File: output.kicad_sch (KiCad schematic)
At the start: 76 parts, among them Q10 AO4407A, Q11 2N7002, Q12 MMBT3904, Q13 2N7002, Q14 2N7002, Q15 2N7002, Q16 2N7002, Q17 2N7002, Q18 MMBT3904, Q19 AO4407A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

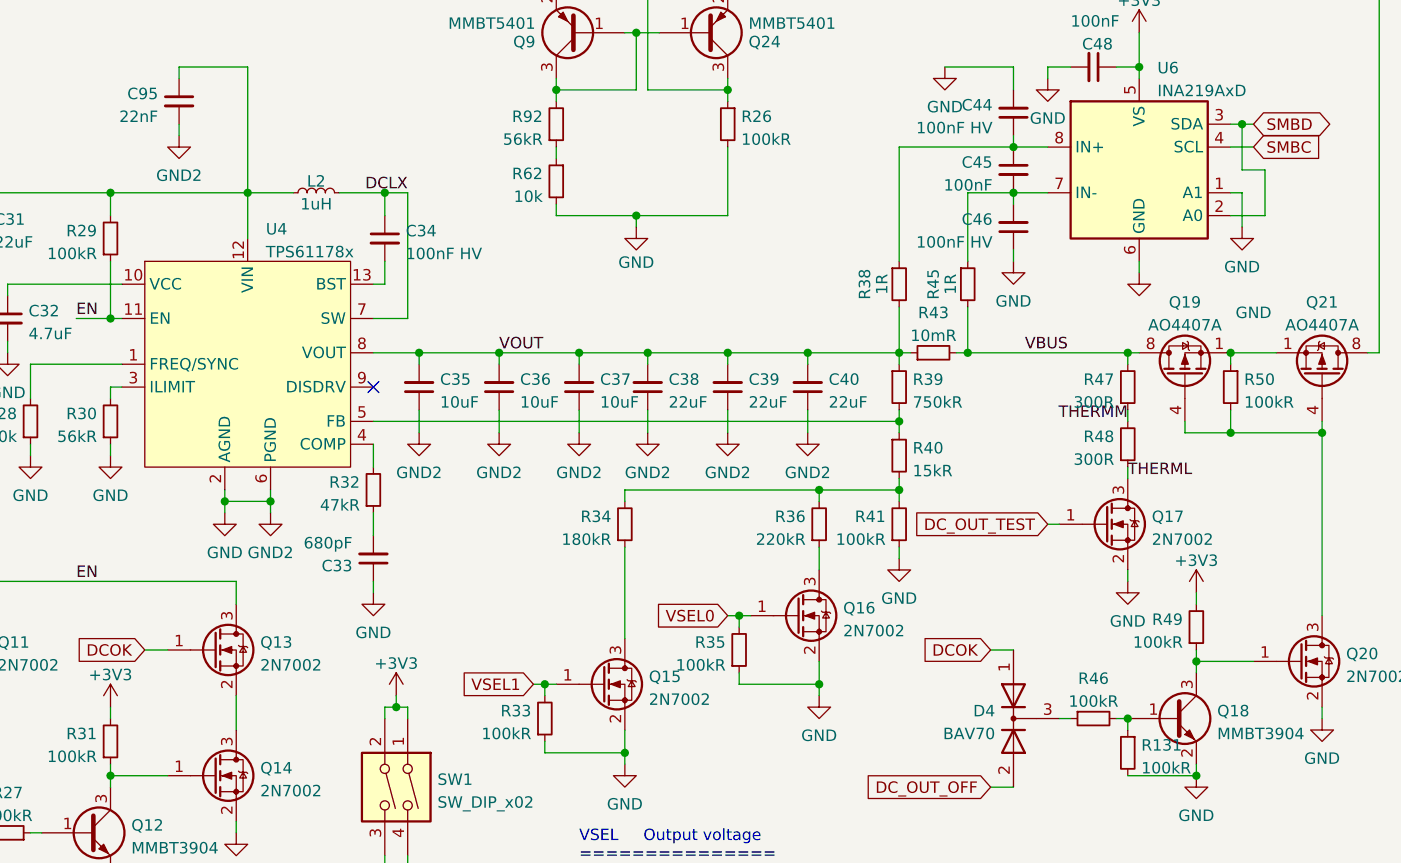
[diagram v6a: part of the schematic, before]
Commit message: Fix remaining RevB bugs
 - DNP Q13 by default to ensure uninterrupted power power delivery
 - Use lower resistance load resistors for DC step-up selftest
 - Add edge rails to support JLCPCB standard assembly

Unfortuantely JLCPCB does not seems to offer ESP32 WROOMs anymore for
economic PCBA. Thus edge-rails have been added to support standard PCBA.
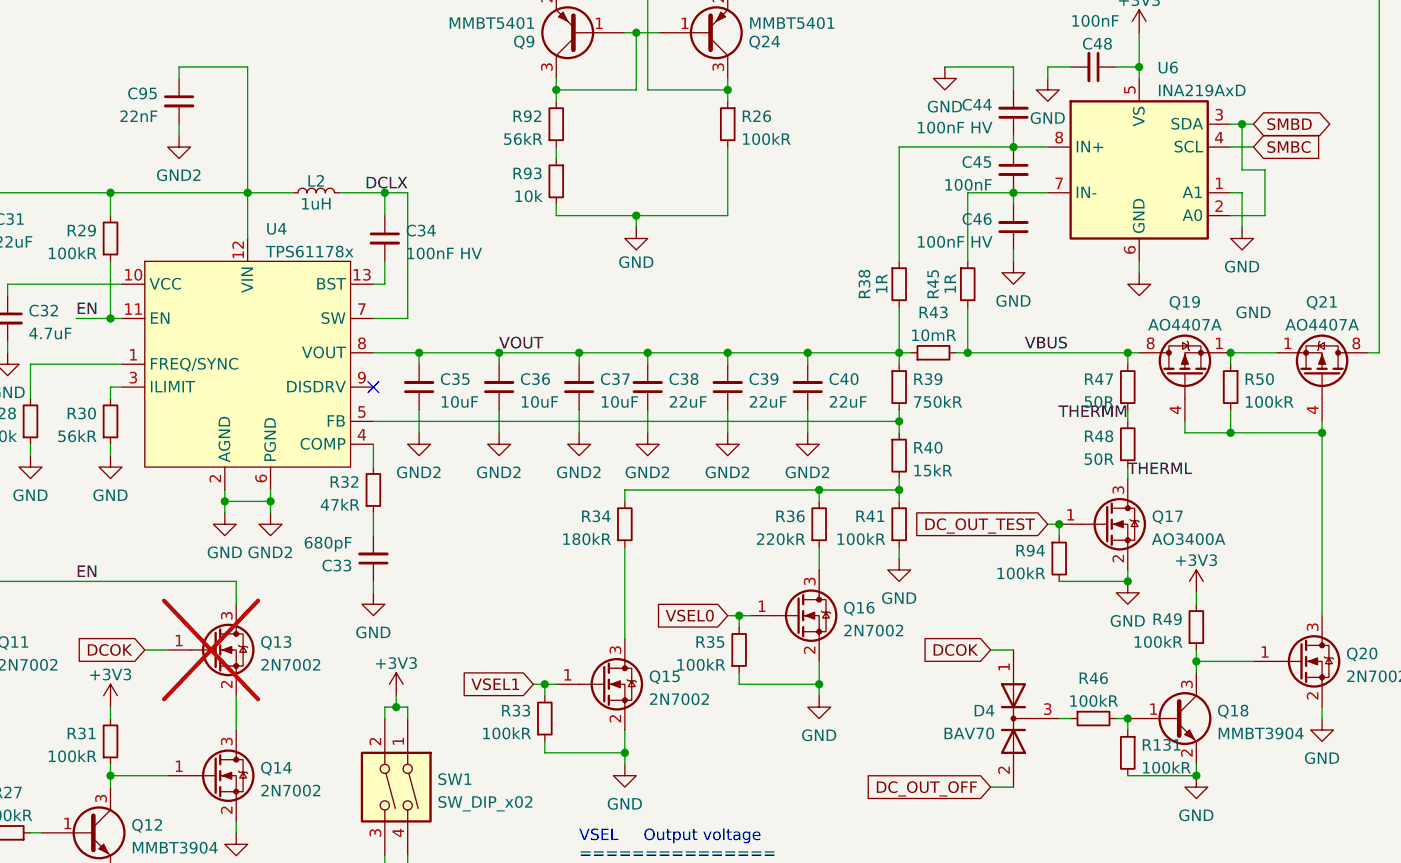
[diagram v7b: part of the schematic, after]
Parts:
- added R94: 100kR, Resistor_SMD:R_0402_1005Metric, symbol Device:R_Small
- Q13: now not fitted; now left out of the parts list
- Q17: value 2N7002 -> AO3400A; LCSC C8545 -> C20917
- R47, R48: value 300R -> 50R; footprint Resistor_SMD:R_1206_3216Metric -> Resistor_SMD:R_2512_6332Metric; LCSC C17887 -> C25487
- renumbered R62 to R93
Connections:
- net DC_OUT_TEST: now also R94.1
- net GND: now also R94.2
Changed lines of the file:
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@@
 (kicad_sch (version 20230121) (generator eeschema)
   (paper "A4")
+  (junction (at 179.07 123.19) (diameter 0) (color 0 0 0 0)
+  )
   (junction (at 194.31 138.43) (diameter 0) (color 0 0 0 0)
   )
@@
   (junction (at 86.36 120.65) (diameter 0) (color 0 0 0 0)
   )
+  (junction (at 186.69 129.54) (diameter 0) (color 0 0 0 0)
+  )
   (junction (at 208.28 113.03) (diameter 0) (color 0 0 0 0)
   )
@@
     (stroke (width 0) (type default))
   )
+  (wire (pts (xy 179.07 123.19) (xy 179.07 124.46))
+    (stroke (width 0) (type default))
+  )
   (wire (pts (xy 198.12 78.74) (xy 199.39 78.74))
     (stroke (width 0) (type default))
@@
     (stroke (width 0) (type default))
   )
+  (wire (pts (xy 179.07 129.54) (xy 186.69 129.54))
+    (stroke (width 0) (type default))
+  )
   (wire (pts (xy 73.66 100.33) (xy 74.93 100.33))
     (stroke (width 0) (type default))
@@
       (effects (font (size 1.27 1.27)) (justify left))
     )
-    (property "Value" "2N7002" (at 189.357 124.8922 0)
+    (property "Value" "AO3400A" (at 189.357 124.8922 0)
       (effects (font (size 1.27 1.27)) (justify left))
     )
@@
       (effects (font (size 1.27 1.27)) (justify left) hide)
     )
-    (property "LCSC" "C8545" (at 184.15 123.19 0)
+    (property "LCSC" "C20917" (at 184.15 123.19 0)
       (effects (font (size 1.27 1.27)) hide)
     )
@@
       (effects (font (size 1.27 1.27)) (justify right))
     )
-    (property "Value" "300R" (at 185.1914 109.6522 0)
+    (property "Value" "50R" (at 185.1914 109.6522 0)
       (effects (font (size 1.27 1.27)) (justify right))
     )
-    (property "Footprint" "Resistor_SMD:R_1206_3216Metric" (at 186.69 107.95 0)
+    (property "Footprint" "Resistor_SMD:R_2512_6332Metric" (at 186.69 107.95 0)
       (effects (font (size 1.27 1.27)) hide)
     )
@@
       (effects (font (size 1.27 1.27)) hide)
     )
-    (property "LCSC" "C17887" (at 186.69 107.95 90)
+    (property "LCSC" "C25487" (at 186.69 107.95 90)
       (effects (font (size 1.27 1.27)) hide)
     )
@@
   )
   (symbol (lib_id "Transistor_FET:2N7002") (at 85.09 137.16 0) (unit 1)
-    (in_bom yes) (on_board yes) (dnp no) (fields_autoplaced)
+    (in_bom no) (on_board yes) (dnp yes) (fields_autoplaced)
     (property "Reference" "Q13" (at 90.297 136.3253 0)
       (effects (font (size 1.27 1.27)) (justify left))
@@
   (symbol (lib_id "Device:R_Small") (at 123.19 85.09 0) (mirror y) (unit 1)
     (in_bom yes) (on_board yes) (dnp no)
-    (property "Reference" "R62" (at 121.6914 84.2553 0)
+    (property "Reference" "R93" (at 121.6914 84.2553 0)
       (effects (font (size 1.27 1.27)) (justify left))
     )
@@
     (instances
       (project "dc-usv"
-        (path "/6c28c5fe-ba66-416c-85ca-0e0cb5063819/a06395f1-7afb-45e9-b1be-eb1d60bae674"
-          (reference "R62") (unit 1)
-        )
         (path "/6c28c5fe-ba66-416c-85ca-0e0cb5063819/4ce9e4d8-553f-40e6-a397-66d04db306f8"
           (reference "R93") (unit 1)
@@
       (effects (font (size 1.27 1.27)) (justify right))
     )
-    (property "Value" "300R" (at 185.1914 116.0022 0)
+    (property "Value" "50R" (at 185.1914 116.0022 0)
       (effects (font (size 1.27 1.27)) (justify right))
     )
-    (property "Footprint" "Resistor_SMD:R_1206_3216Metric" (at 186.69 114.3 0)
+    (property "Footprint" "Resistor_SMD:R_2512_6332Metric" (at 186.69 114.3 0)
       (effects (font (size 1.27 1.27)) hide)
     )
@@
       (effects (font (size 1.27 1.27)) hide)
     )
-    (property "LCSC" "C17887" (at 186.69 114.3 90)
+    (property "LCSC" "C25487" (at 186.69 114.3 90)
       (effects (font (size 1.27 1.27)) hide)
     )
@@
         )
       )
+    )
+  )
+  (symbol (lib_id "Device:R_Small") (at 179.07 127 0) (unit 1)
+    (in_bom yes) (on_board yes) (dnp no)
+    (property "Reference" "R94" (at 177.5714 126.1653 0)
+      (effects (font (size 1.27 1.27)) (justify right))
+    )
+    (property "Value" "100kR" (at 177.5714 128.7022 0)
+      (effects (font (size 1.27 1.27)) (justify right))
+    )
+    (property "Footprint" "Resistor_SMD:R_0402_1005Metric" (at 179.07 127 0)
+      (effects (font (size 1.27 1.27)) hide)
+    )
+    (property "Datasheet" "~" (at 179.07 127 0)
+      (effects (font (size 1.27 1.27)) hide)
+    )
+    (property "LCSC" "C25741" (at 179.07 127 0)
+      (effects (font (size 1.27 1.27)) hide)
+    )
+    (pin "1")
+    (pin "2")
+    (instances
+      (project "dc-usv"
+        (path "/6c28c5fe-ba66-416c-85ca-0e0cb5063819/4ce9e4d8-553f-40e6-a397-66d04db306f8"
+          (reference "R94") (unit 1)
+        )
+      )
